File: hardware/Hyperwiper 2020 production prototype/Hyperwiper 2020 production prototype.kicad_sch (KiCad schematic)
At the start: 24 parts, among them J1 Conn_01x05, K1 Main Power relay, K2 Wiper control relay, Q1 PN2222A, SW1 ON-OFF, SW2 SW_Reed, U1 Teensy4.0, U3 XBEE-socket

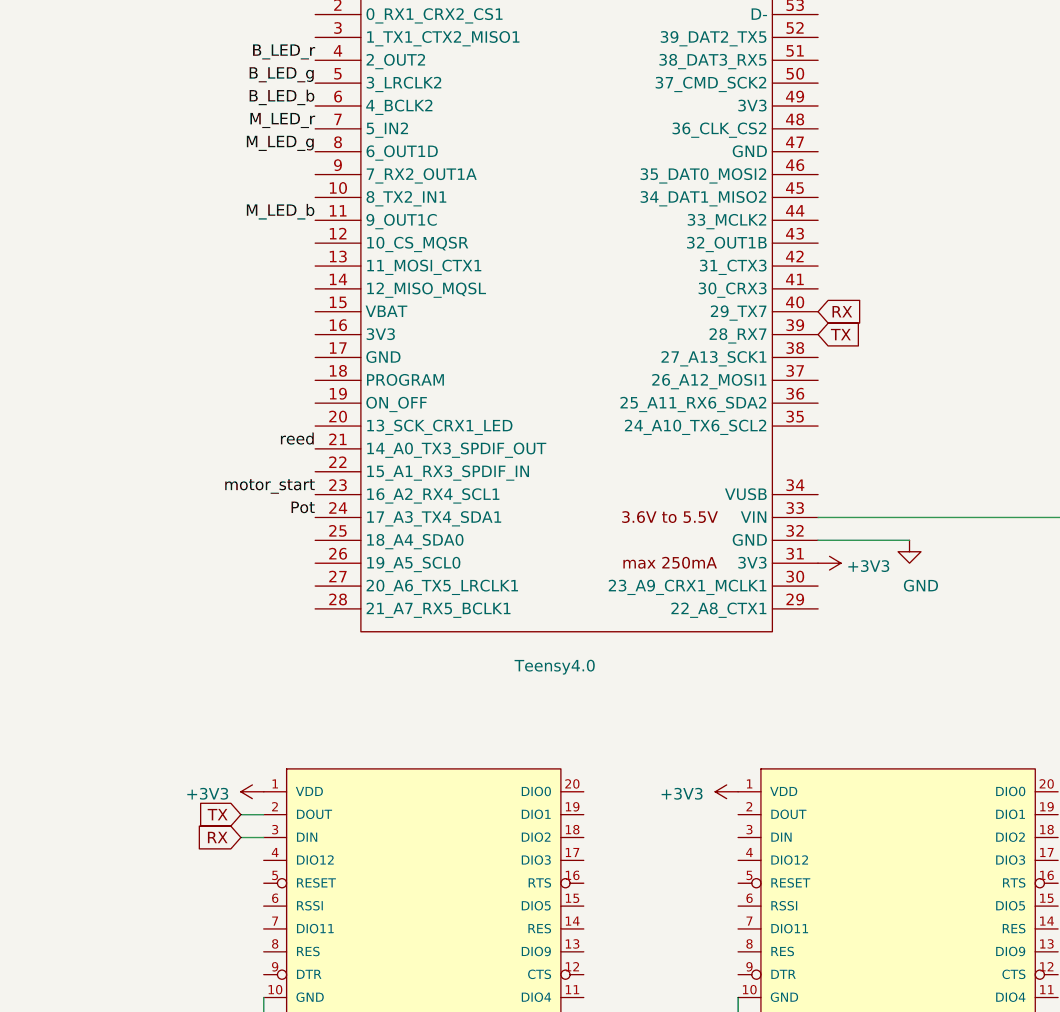
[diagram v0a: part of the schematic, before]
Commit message: Updated board with Xbee BLE setup
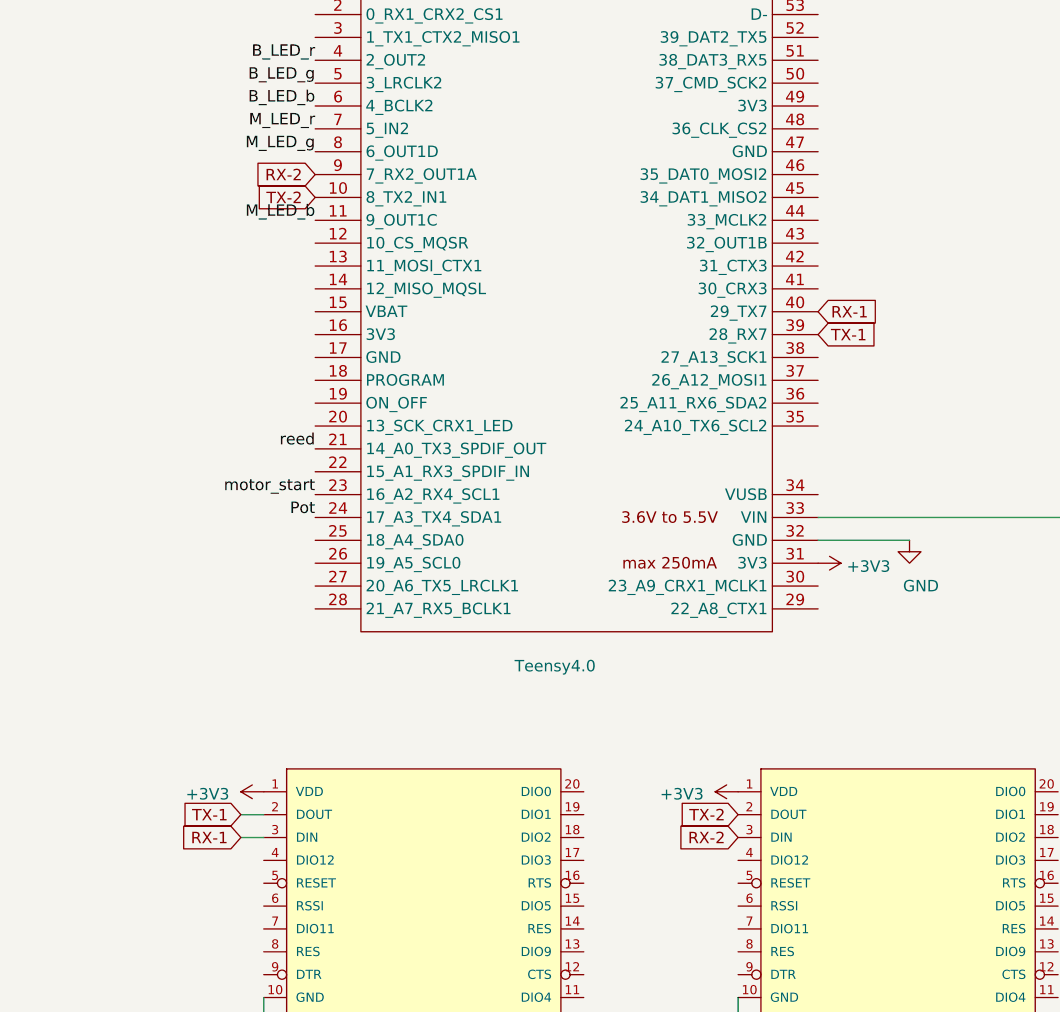
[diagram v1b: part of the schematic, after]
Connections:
- net TX-2: now reaches U1.10 (8_TX2_IN1)
- net TX-2: now also JP2.2 (DOUT)
- net RX-2: now reaches U1.9 (7_RX2_OUT1A)
- net RX-2: now also JP2.3 (DIN)
- net RX renamed RX-1
- net TX renamed TX-1
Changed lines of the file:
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@@
     (effects (font (size 1.27 1.27)) (justify right bottom))
   )
-  (global_label "TX" (shape input) (at 43.815 116.84 180)    (property "Intersheet References" "${INTERSHEET_REFS}" (id 0) (at 37.7008 116.7606 0)
+  (global_label "TX-1" (shape input) (at 43.815 116.84 180)    (property "Intersheet References" "${INTERSHEET_REFS}" (id 0) (at 34.9189 116.7606 0)
       (effects (font (size 1.27 1.27)) (justify right) hide)
     )
     (effects (font (size 1.27 1.27)) (justify right))
   )
-  (global_label "RX" (shape input) (at 43.815 119.38 180)    (property "Intersheet References" "${INTERSHEET_REFS}" (id 0) (at 37.3984 119.3006 0)
+  (global_label "RX-1" (shape input) (at 43.815 119.38 180)    (property "Intersheet References" "${INTERSHEET_REFS}" (id 0) (at 34.6165 119.3006 0)
       (effects (font (size 1.27 1.27)) (justify right) hide)
     )
     (effects (font (size 1.27 1.27)) (justify right))
   )
-  (global_label "RX" (shape input) (at 107.95 60.96 0)    (property "Intersheet References" "${INTERSHEET_REFS}" (id 0) (at 114.3666 61.0394 0)
+  (global_label "RX-2" (shape input) (at 52.07 45.72 180)    (property "Intersheet References" "${INTERSHEET_REFS}" (id 0) (at 42.8715 45.6406 0)
+      (effects (font (size 1.27 1.27)) (justify right) hide)
+    )
+    (effects (font (size 1.27 1.27)) (justify right))
+  )
+  (global_label "TX-2" (shape input) (at 52.07 48.26 180)    (property "Intersheet References" "${INTERSHEET_REFS}" (id 0) (at 43.1739 48.1806 0)
+      (effects (font (size 1.27 1.27)) (justify right) hide)
+    )
+    (effects (font (size 1.27 1.27)) (justify right))
+  )
+  (global_label "TX-2" (shape input) (at 99.06 116.84 180)    (property "Intersheet References" "${INTERSHEET_REFS}" (id 0) (at 90.1639 116.7606 0)
+      (effects (font (size 1.27 1.27)) (justify right) hide)
+    )
+    (effects (font (size 1.27 1.27)) (justify right))
+  )
+  (global_label "RX-2" (shape input) (at 99.06 119.38 180)    (property "Intersheet References" "${INTERSHEET_REFS}" (id 0) (at 89.8615 119.3006 0)
+      (effects (font (size 1.27 1.27)) (justify right) hide)
+    )
+    (effects (font (size 1.27 1.27)) (justify right))
+  )
+  (global_label "RX-1" (shape input) (at 107.95 60.96 0)    (property "Intersheet References" "${INTERSHEET_REFS}" (id 0) (at 117.1485 60.8806 0)
       (effects (font (size 1.27 1.27)) (justify left) hide)
     )
     (effects (font (size 1.27 1.27)) (justify left))
   )
-  (global_label "TX" (shape input) (at 107.95 63.5 0)    (property "Intersheet References" "${INTERSHEET_REFS}" (id 0) (at 114.0642 63.5794 0)
+  (global_label "TX-1" (shape input) (at 107.95 63.5 0)    (property "Intersheet References" "${INTERSHEET_REFS}" (id 0) (at 116.8461 63.4206 0)
       (effects (font (size 1.27 1.27)) (justify left) hide)
     )

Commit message: Updated board
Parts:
- added C2, C3: 100uF, Capacitor_THT:CP_Radial_D12.5mm_P7.50mm, symbol Device:CP
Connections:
- net +3V3: now also RV1.3, C2.1
- net 5V: now also C3.1; no longer RV1.3
- net GND: now also C2.2, C3.2
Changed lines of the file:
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@@
   )
   (junction (at 179.07 20.32) (diameter 0.259) (color 0 0 0 0))
+  (junction (at 207.645 33.02) (diameter 0.259) (color 0 0 0 0))
+  (junction (at 213.36 20.32) (diameter 0.259) (color 0 0 0 0))
   (junction (at 217.17 54.61) (diameter 0.259) (color 0 0 0 0))
   (junction (at 228.6 46.99) (diameter 0.259) (color 0 0 0 0))
@@
     (stroke (width 0) (type solid) (color 0 0 0 0))
   )
-  (wire (pts (xy 179.07 20.32) (xy 248.92 20.32))
+  (wire (pts (xy 179.07 20.32) (xy 213.36 20.32))
     (stroke (width 0) (type solid) (color 0 0 0 0))
   )
@@
     (stroke (width 0) (type solid) (color 0 0 0 0))
   )
+  (wire (pts (xy 203.2 33.02) (xy 207.645 33.02))
+    (stroke (width 0) (type solid) (color 0 0 0 0))
+  )
   (wire (pts (xy 204.47 54.61) (xy 217.17 54.61))
     (stroke (width 0) (type solid) (color 0 0 0 0))
   )
   (wire (pts (xy 204.47 55.88) (xy 204.47 54.61))
+    (stroke (width 0) (type solid) (color 0 0 0 0))
+  )
+  (wire (pts (xy 207.645 33.02) (xy 207.645 36.195))
+    (stroke (width 0) (type solid) (color 0 0 0 0))
+  )
+  (wire (pts (xy 207.645 33.02) (xy 213.36 33.02))
+    (stroke (width 0) (type solid) (color 0 0 0 0))
+  )
+  (wire (pts (xy 213.36 20.32) (xy 213.36 25.4))
+    (stroke (width 0) (type solid) (color 0 0 0 0))
+  )
+  (wire (pts (xy 213.36 20.32) (xy 248.92 20.32))
     (stroke (width 0) (type solid) (color 0 0 0 0))
   )
@@
     (effects (font (size 1.27 1.27)) (justify right bottom))
   )
-  (label "5V" (at 161.29 152.4 180)
-    (effects (font (size 1.27 1.27)) (justify right bottom))
-  )
   (label "reed" (at 236.22 109.855 180)
     (effects (font (size 1.27 1.27)) (justify right bottom))
@@
     )
   )
+  (symbol (lib_id "power:+3V3") (at 161.29 152.4 270) (unit 1)
+    (in_bom yes) (on_board yes)
+    (property "Reference" "#PWR0116" (id 0) (at 157.48 152.4 0)
+      (effects (font (size 1.27 1.27)) hide)
+    )
+    (property "Value" "+3V3" (id 1) (at 164.4651 152.7683 90)
+      (effects (font (size 1.27 1.27)) (justify left))
+    )
+    (property "Footprint" "" (id 2) (at 161.29 152.4 0)
+      (effects (font (size 1.27 1.27)) hide)
+    )
+    (property "Datasheet" "" (id 3) (at 161.29 152.4 0)
+      (effects (font (size 1.27 1.27)) hide)
+    )
+  )
+  (symbol (lib_id "power:+3V3") (at 203.2 25.4 90) (unit 1)
+    (in_bom yes) (on_board yes)
+    (property "Reference" "#PWR01" (id 0) (at 207.01 25.4 0)
+      (effects (font (size 1.27 1.27)) hide)
+    )
+    (property "Value" "+3V3" (id 1) (at 200.0249 25.0317 90)
+      (effects (font (size 1.27 1.27)) (justify left))
+    )
+    (property "Footprint" "" (id 2) (at 203.2 25.4 0)
+      (effects (font (size 1.27 1.27)) hide)
+    )
+    (property "Datasheet" "" (id 3) (at 203.2 25.4 0)
+      (effects (font (size 1.27 1.27)) hide)
+    )
+  )
   (symbol (lib_id "power:GND") (at 46.355 142.875 0) (unit 1)
     (in_bom yes) (on_board yes)
@@
     )
     (property "Datasheet" "" (id 3) (at 199.39 142.24 0)
+      (effects (font (size 1.27 1.27)) hide)
+    )
+  )
+  (symbol (lib_id "power:GND") (at 207.645 36.195 0) (unit 1)
+    (in_bom yes) (on_board yes)
+    (property "Reference" "#PWR02" (id 0) (at 207.645 42.545 0)
+      (effects (font (size 1.27 1.27)) hide)
+    )
+    (property "Value" "GND" (id 1) (at 210.82 37.465 0))
+    (property "Footprint" "" (id 2) (at 207.645 36.195 0)
+      (effects (font (size 1.27 1.27)) hide)
+    )
+    (property "Datasheet" "" (id 3) (at 207.645 36.195 0)
       (effects (font (size 1.27 1.27)) hide)
     )
@@
     )
     (property "Datasheet" "~" (id 3) (at 245.11 88.9 0)
+      (effects (font (size 1.27 1.27)) hide)
+    )
+  )
+  (symbol (lib_id "Device:CP") (at 203.2 29.21 0) (unit 1)
+    (in_bom yes) (on_board yes)
+    (property "Reference" "C2" (id 0) (at 206.1211 28.0606 0)
+      (effects (font (size 1.27 1.27)) (justify left))
+    )
+    (property "Value" "100uF" (id 1) (at 206.1211 30.3593 0)
+      (effects (font (size 1.27 1.27)) (justify left))
+    )
+    (property "Footprint" "Capacitor_THT:CP_Radial_D12.5mm_P7.50mm" (id 2) (at 204.1652 33.02 0)
+      (effects (font (size 1.27 1.27)) hide)
+    )
+    (property "Datasheet" "~" (id 3) (at 203.2 29.21 0)
+      (effects (font (size 1.27 1.27)) hide)
+    )
+  )
+  (symbol (lib_id "Device:CP") (at 213.36 29.21 0) (unit 1)
+    (in_bom yes) (on_board yes)
+    (property "Reference" "C3" (id 0) (at 216.2811 28.0606 0)
+      (effects (font (size 1.27 1.27)) (justify left))
+    )
+    (property "Value" "100uF" (id 1) (at 216.2811 30.3593 0)
+      (effects (font (size 1.27 1.27)) (justify left))
+    )
+    (property "Footprint" "Capacitor_THT:CP_Radial_D12.5mm_P7.50mm" (id 2) (at 214.325 33.02 0)
+      (effects (font (size 1.27 1.27)) hide)
+    )
+    (property "Datasheet" "~" (id 3) (at 213.36 29.21 0)
       (effects (font (size 1.27 1.27)) hide)
     )
@@
   )
   (symbol_instances
+    (path "/e8a75eb0-c244-415b-afbc-d6992691e712"
+      (reference "#PWR01") (unit 1) (value "+3V3") (footprint "")
+    )
+    (path "/1523e18f-a60a-446e-95ea-88795e5fc309"
+      (reference "#PWR02") (unit 1) (value "GND") (footprint "")
+    )
     (path "/9ecc80e1-69b7-4287-95ed-bfffa7d18207"
       (reference "#PWR0101") (unit 1) (value "GND") (footprint "")
@@
       (reference "#PWR0115") (unit 1) (value "GND") (footprint "")
     )
+    (path "/767b37fe-2445-4ff7-86c2-b8fae626c28d"
+      (reference "#PWR0116") (unit 1) (value "+3V3") (footprint "")
+    )
     (path "/bc80e3ce-b48d-40fd-b22c-6384e7899540"
       (reference "C1") (unit 1) (value "0.1uF") (footprint "Capacitor_THT:C_Rect_L7.0mm_W2.5mm_P5.00mm")
     )
+    (path "/a3df5c38-cb40-4288-94fc-7fa0713cdfdf"
+      (reference "C2") (unit 1) (value "100uF") (footprint "Capacitor_THT:CP_Radial_D12.5mm_P7.50mm")
+    )
+    (path "/845347af-56a0-4cb3-b8db-952808318f9a"
+      (reference "C3") (unit 1) (value "100uF") (footprint "Capacitor_THT:CP_Radial_D12.5mm_P7.50mm")
+    )
     (path "/2723ac12-21fb-4eb0-b91d-4ea3a28c8ae0"

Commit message: Update files
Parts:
- U3: value XBEE-socket -> Voltage regulator
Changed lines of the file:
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@@
     (in_bom yes) (on_board yes)
     (property "Reference" "U3" (id 0) (at 241.3 21.59 0))
-    (property "Value" "XBEE-socket" (id 1) (at 241.3 24.13 0))
+    (property "Value" "Voltage regulator" (id 1) (at 241.3 24.13 0))
     (property "Footprint" "Package_TO_SOT_THT:TO-220-3_Vertical" (id 2) (at 241.935 33.02 0)
       (effects (font (size 1.27 1.27) italic) (justify left) hide)
@@
     )
     (path "/f9d2509a-a206-4349-9d2a-528f7b1ec6de"
-      (reference "U3") (unit 1) (value "XBEE-socket") (footprint "Package_TO_SOT_THT:TO-220-3_Vertical")
-    )
-  )
+      (reference "U3") (unit 1) (value "Voltage regulator") (footprint "Package_TO_SOT_THT:TO-220-3_Vertical")
+    )
+  )

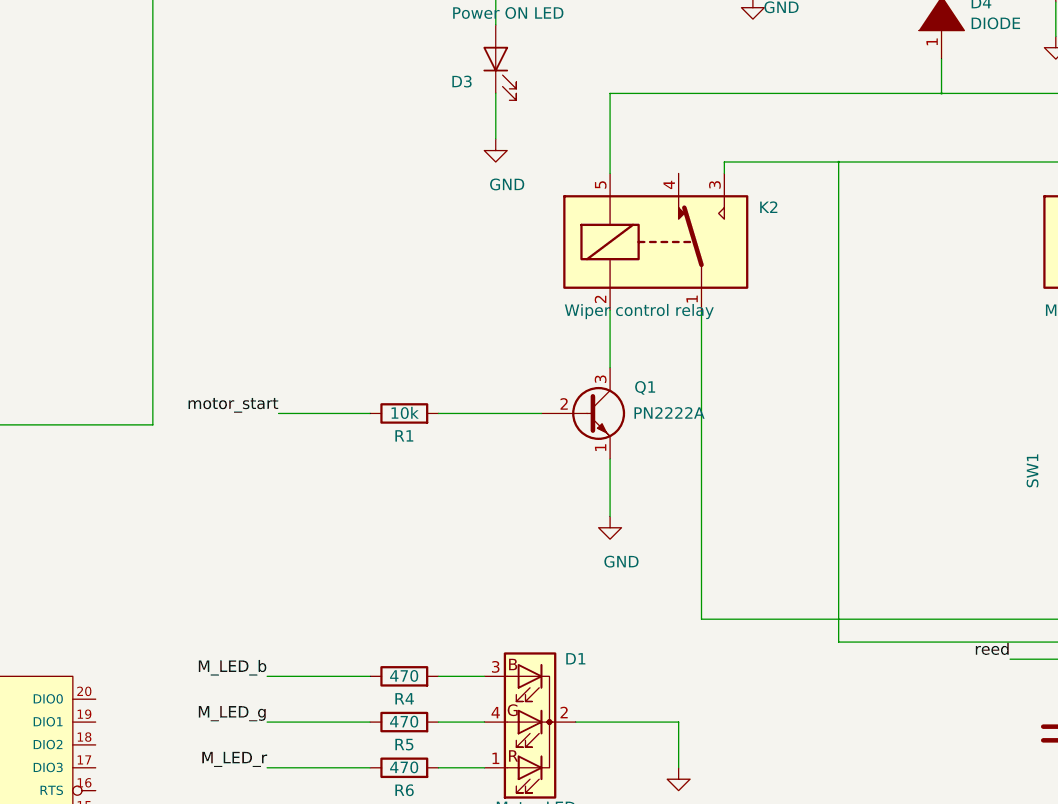
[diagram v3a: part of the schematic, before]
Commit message: Updated board with MOSFET IRF540N
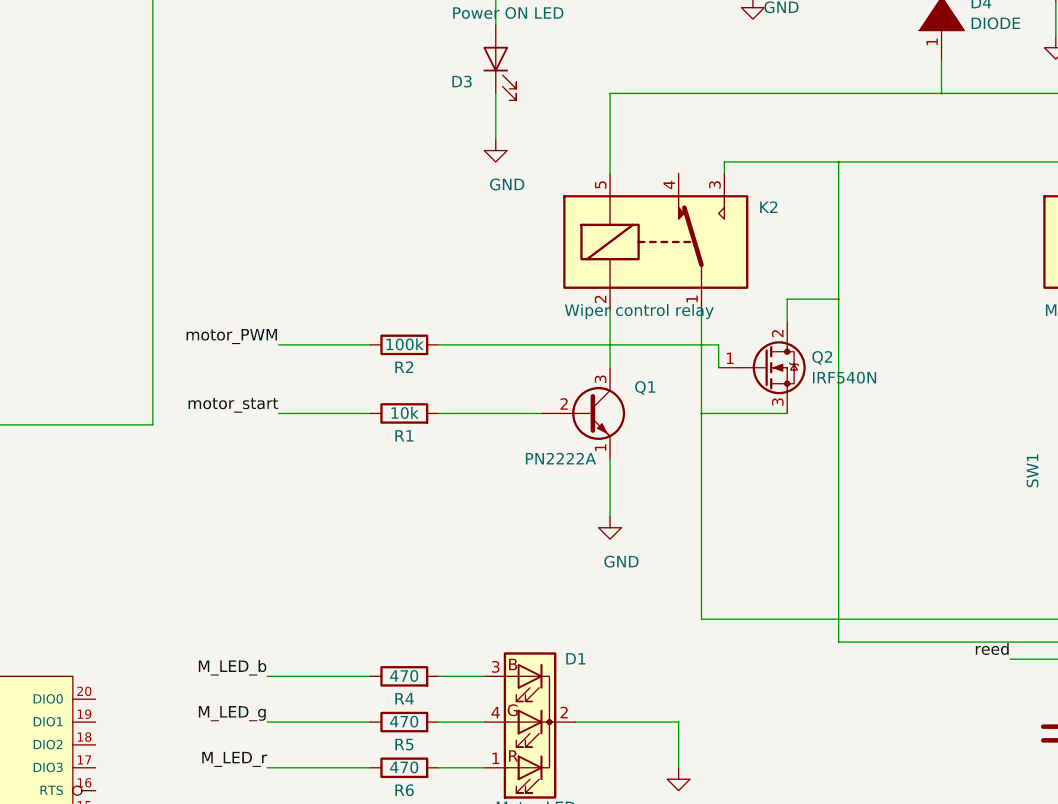
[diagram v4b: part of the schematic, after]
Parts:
- added Q2: IRF540N, Package_TO_SOT_THT:TO-220-3_Vertical, symbol Transistor_FET:IRF540N
- added R2: 100k, Resistor_THT:R_Axial_DIN0207_L6.3mm_D2.5mm_P10.16mm_Horizontal, symbol Device:R
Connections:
- net at J1.1 (Pin_1), K1.1, K1.5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: now also Q2.3 (S)
- net at J1.2 (Pin_2), K1.4, K2.3: now also Q2.2 (D)
- new net: Q2.1 (G), R2.2
- new net motor_PWM: R2.1
